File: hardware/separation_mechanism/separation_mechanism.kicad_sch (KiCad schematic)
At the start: 41 parts, among them J1 Conn_01x02_Socket, J3 USB3_B, J4 Conn_01x02_Socket, J5 Micro_SD_Card_Det_Hirose_DM3AT, Q1 AO3400A, U1 L7805, U2 SAM-M10Q-00B, U3 SHT4x, U4 DPS368, U5 E22-900T30D_E220-900T22S(JP)_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, U6 FT4232H

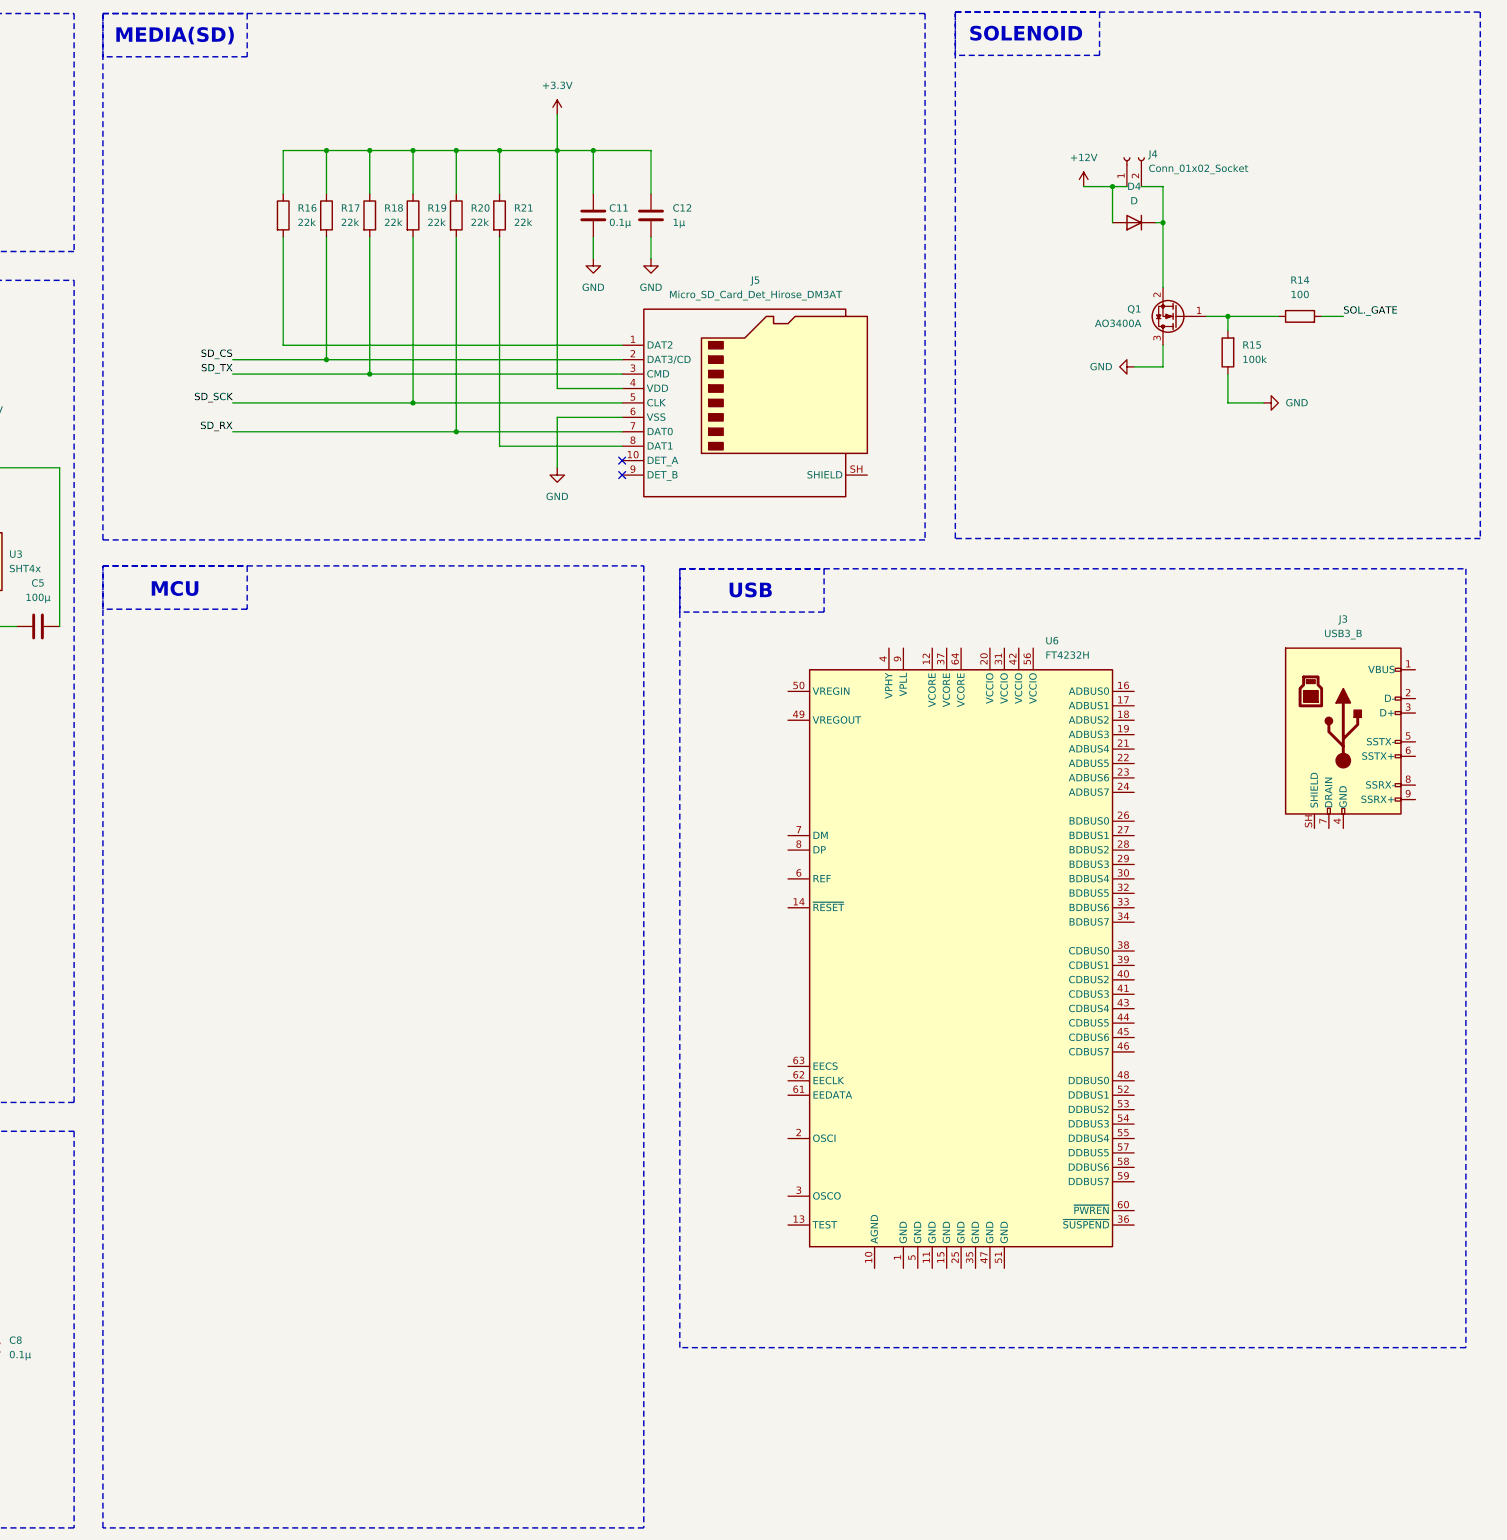
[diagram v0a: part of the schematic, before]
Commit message: feat(scm): USB-UART Converter
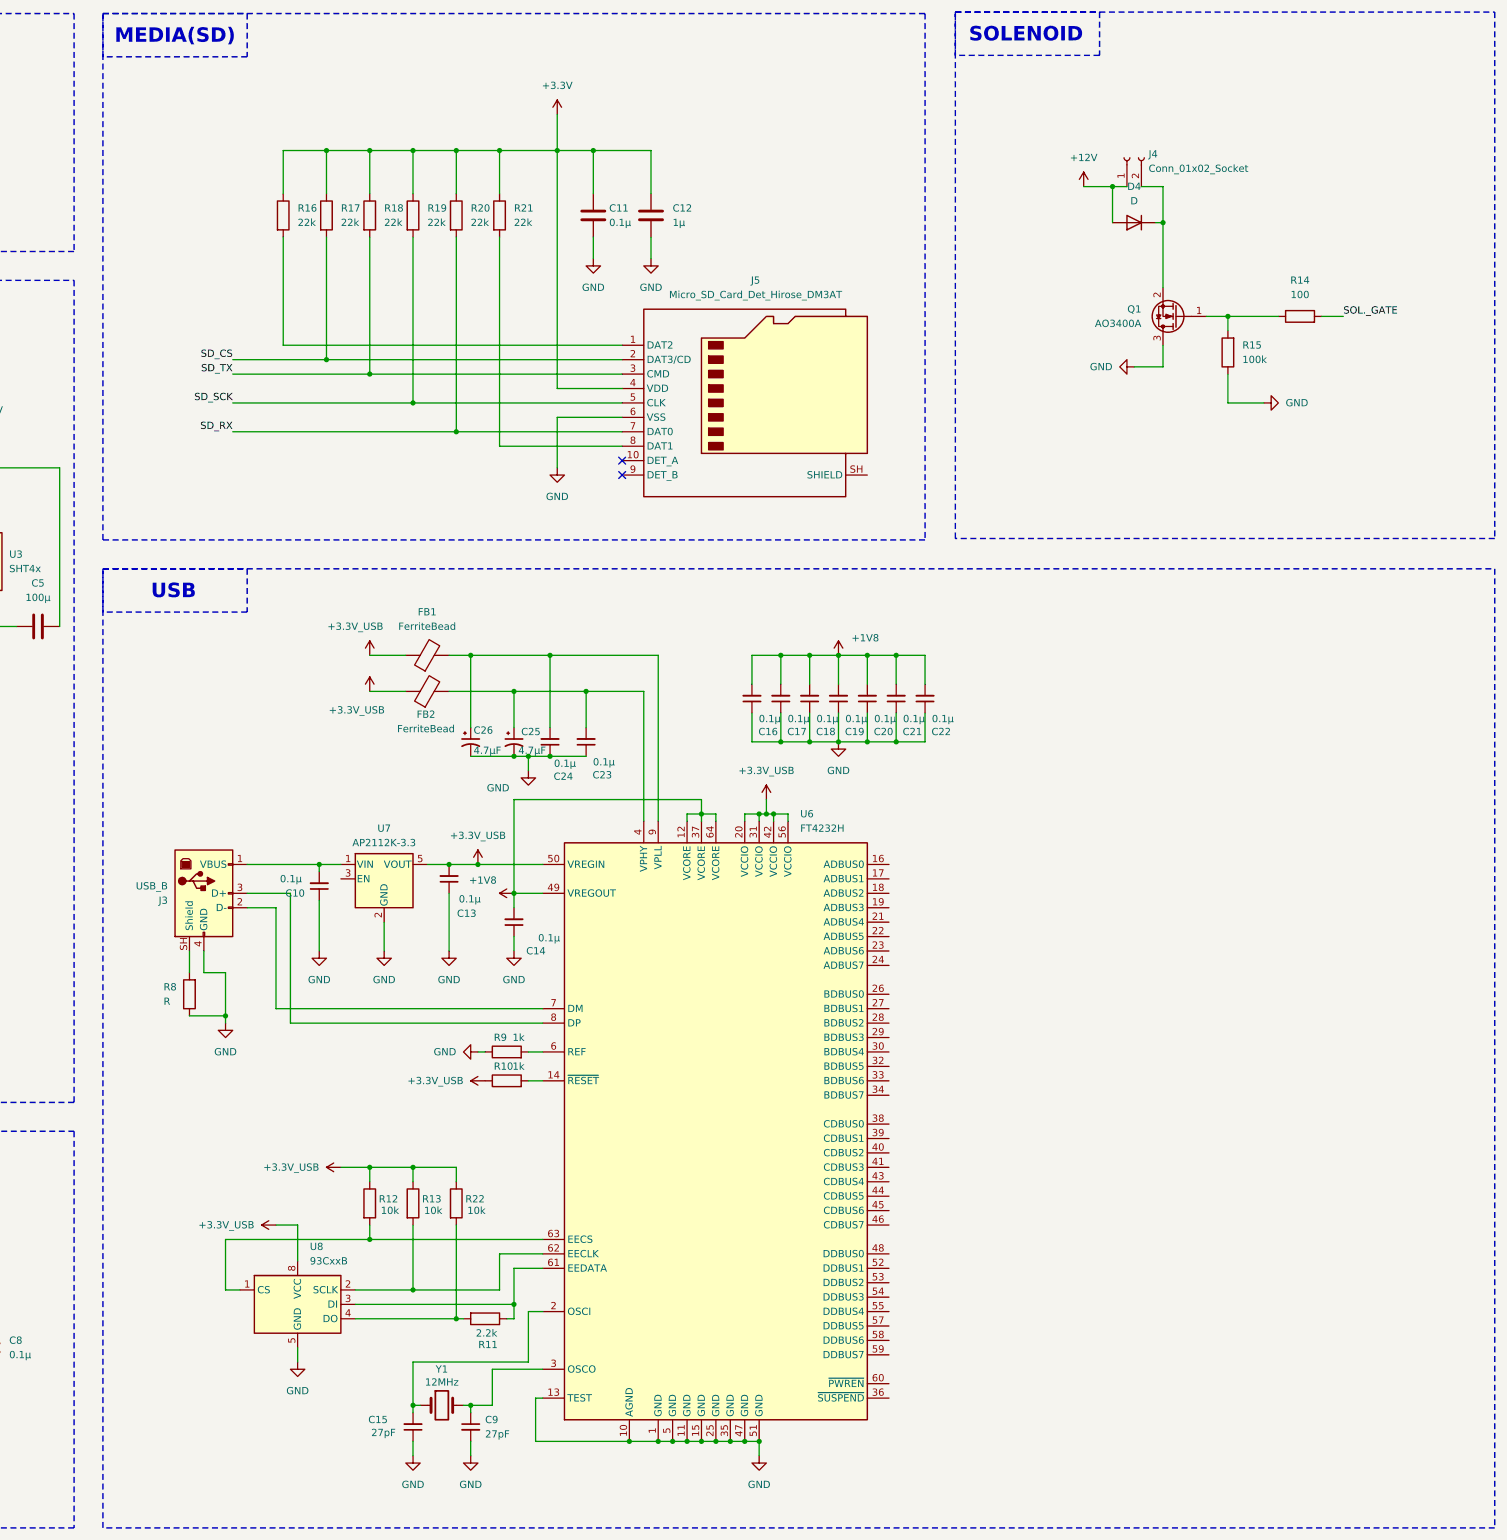
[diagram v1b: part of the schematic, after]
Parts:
- removed J3: USB3_B, symbol Connector:USB3_B
- added C10, C13, C14, C16, C17, C18, C19, C20, C21, C22, C23, C24: 0.1μ, symbol Device:C_Small
- added C15, C9: 27pF, symbol Device:C_Small
- added C25, C26: 4.7μF, symbol Device:C_Polarized_Small_US
- added FB1, FB2: FerriteBead, symbol Device:FerriteBead
- added J3: USB_B, symbol Connector:USB_B
- added R10, R9: 1k, symbol Device:R
- added R11: 2.2k, symbol Device:R
- added R12, R13, R22: 10k, symbol Device:R
- added R8: R, symbol Device:R
- added U7: AP2112K-3.3, Package_TO_SOT_SMD:SOT-23-5, symbol Regulator_Linear:AP2112K-3.3
- added U8: 93CxxB, symbol Memory_EEPROM:93CxxB
- added Y1: 12MHz, symbol Device:Crystal
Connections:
- net GND: now also U6.1 (GND), U6.10 (AGND), U6.11 (GND), U6.13 (TEST), U6.15 (GND), U6.25 (GND), U6.35 (GND), U6.47 (GND), U6.5 (GND), U6.51 (GND), C10.1, C13.1, C14.1, C15.1, C16.1, C17.1, C18.1, C19.1, C20.1, C21.1, C22.1, C23.1, C24.1, C25.2, C26.2, C9.2, J3.4 (GND), R8.1, R9.1, U7.2 (GND), U8.5 (GND)
- net +1V8: now reaches U6.12 (VCORE)
- net +1V8: now also U6.37 (VCORE), U6.49 (VREGOUT), U6.64 (VCORE), C14.2, C16.2, C17.2, C18.2, C19.2, C20.2, C21.2, C22.2
- net at U6.14 (~{RESET}): now also R10.2
- net at U6.2 (OSCI): now also C15.2, Y1.1
- net +3.3V_USB: now reaches U6.20 (VCCIO)
- net +3.3V_USB: now also U6.31 (VCCIO), U6.42 (VCCIO), U6.50 (VREGIN), U6.56 (VCCIO), C13.2, FB1.1, FB2.1, R10.1, R12.1, R13.1, R22.1, U7.5 (VOUT), U8.8 (VCC)
- net at U6.3 (OSCO): now also C9.1, Y1.2
- net at U6.4 (VPHY): now also C23.2, C25.1, FB2.2
- net at U6.6 (REF): now also R9.2
- net at U6.61 (EEDATA): now also R11.1, U8.3 (DI)
- net at U6.62 (EECLK): now also R13.2, U8.2 (SCLK)
- net at U6.63 (EECS): now also R12.2, U8.1 (CS)
- net at U6.7 (DM): now also J3.2 (D-)
- net at U6.8 (DP): now also J3.3 (D+)
- net at U6.9 (VPLL): now also C24.2, C26.1, FB1.2
- new net: R11.2, R22.2, U8.4 (DO)
- new net: J3.SH (Shield), R8.2
- new net: C10.2, J3.1 (VBUS), U7.1 (VIN)
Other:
- note removed: "MCU"
- moved on the sheet: U6
